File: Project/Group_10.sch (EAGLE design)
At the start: 20 parts, among them J1 POWER_JACKPTH_LOCK, U1 +12v, U4 TMUX1208

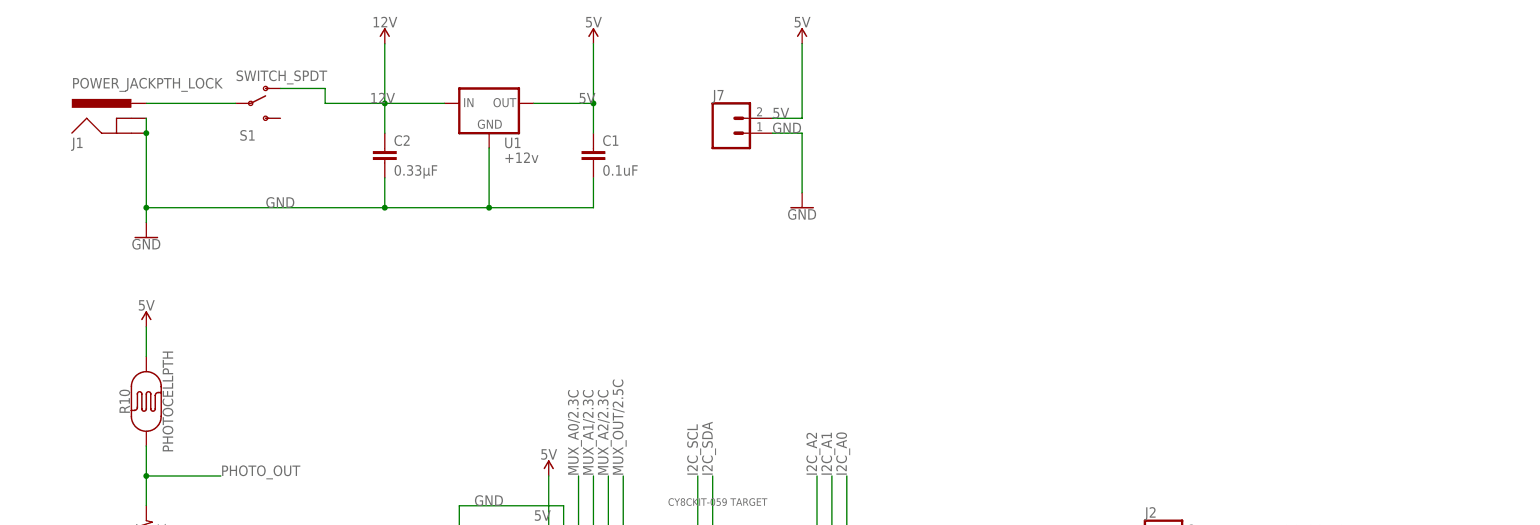
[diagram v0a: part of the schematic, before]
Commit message: Added device TCA9546A to schematic and added value to R1
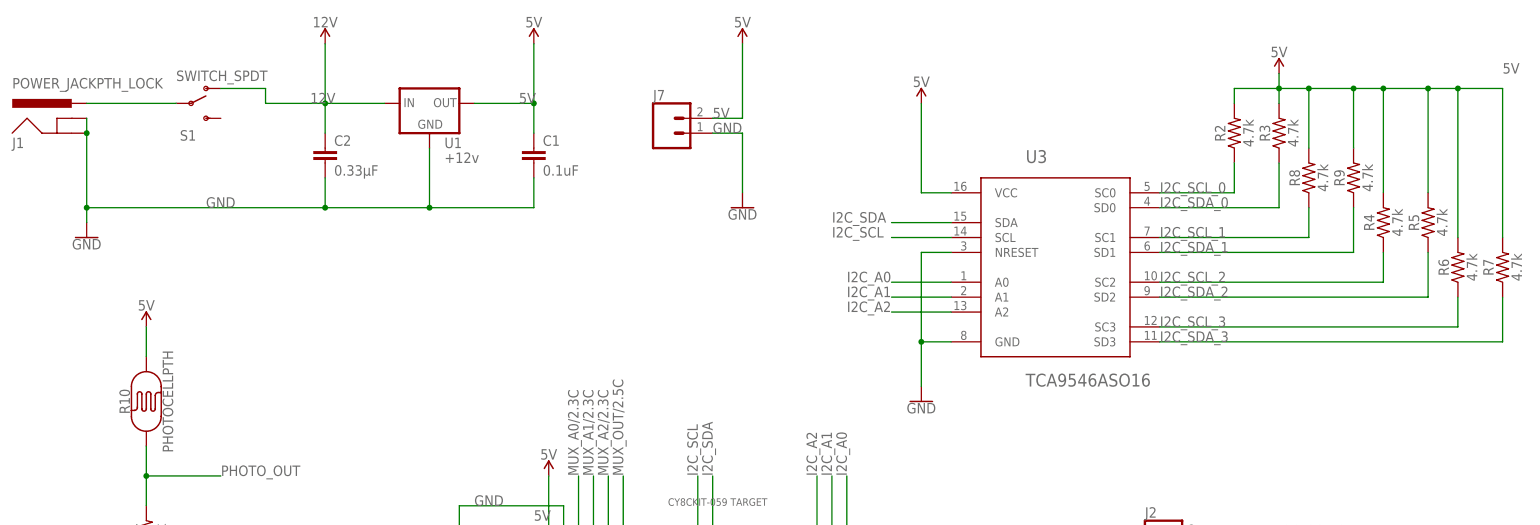
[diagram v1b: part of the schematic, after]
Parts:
- added R2, R3, R4, R5, R6, R7, R8, R9: 4.7k, SparkFun-Resistors:4.7KOHM-0603-1/10W-1%
- added U3: TCA9546ASO16, Group_10_Library:TCA9546ASO16
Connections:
- net 5V: now also R2.2, R3.2, R4.2, R5.2, R6.2, R7.2, R8.2, R9.2, U3.VCC
- net GND: now also U3.GND, U3.NRESET
- net I2C_A0: now also U3.A0
- net I2C_A1: now also U3.A1
- net I2C_A2: now also U3.A2
- net I2C_SCL: now also U3.SCL
- net I2C_SCL_0: now also R2.1, U3.SC0
- net I2C_SCL_1: now also R8.1, U3.SC1
- net I2C_SCL_2: now also R4.1, U3.SC2
- net I2C_SCL_3: now also R6.1, U3.SC3
- net I2C_SDA: now also U3.SDA
- net I2C_SDA_0: now also R3.1, U3.SD0
- net I2C_SDA_1: now also R9.1, U3.SD1
- net I2C_SDA_2: now also R5.1, U3.SD2
- net I2C_SDA_3: now also R7.1, U3.SD3
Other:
- moved on the sheet: C1, C2, J1, J7, S1, U1

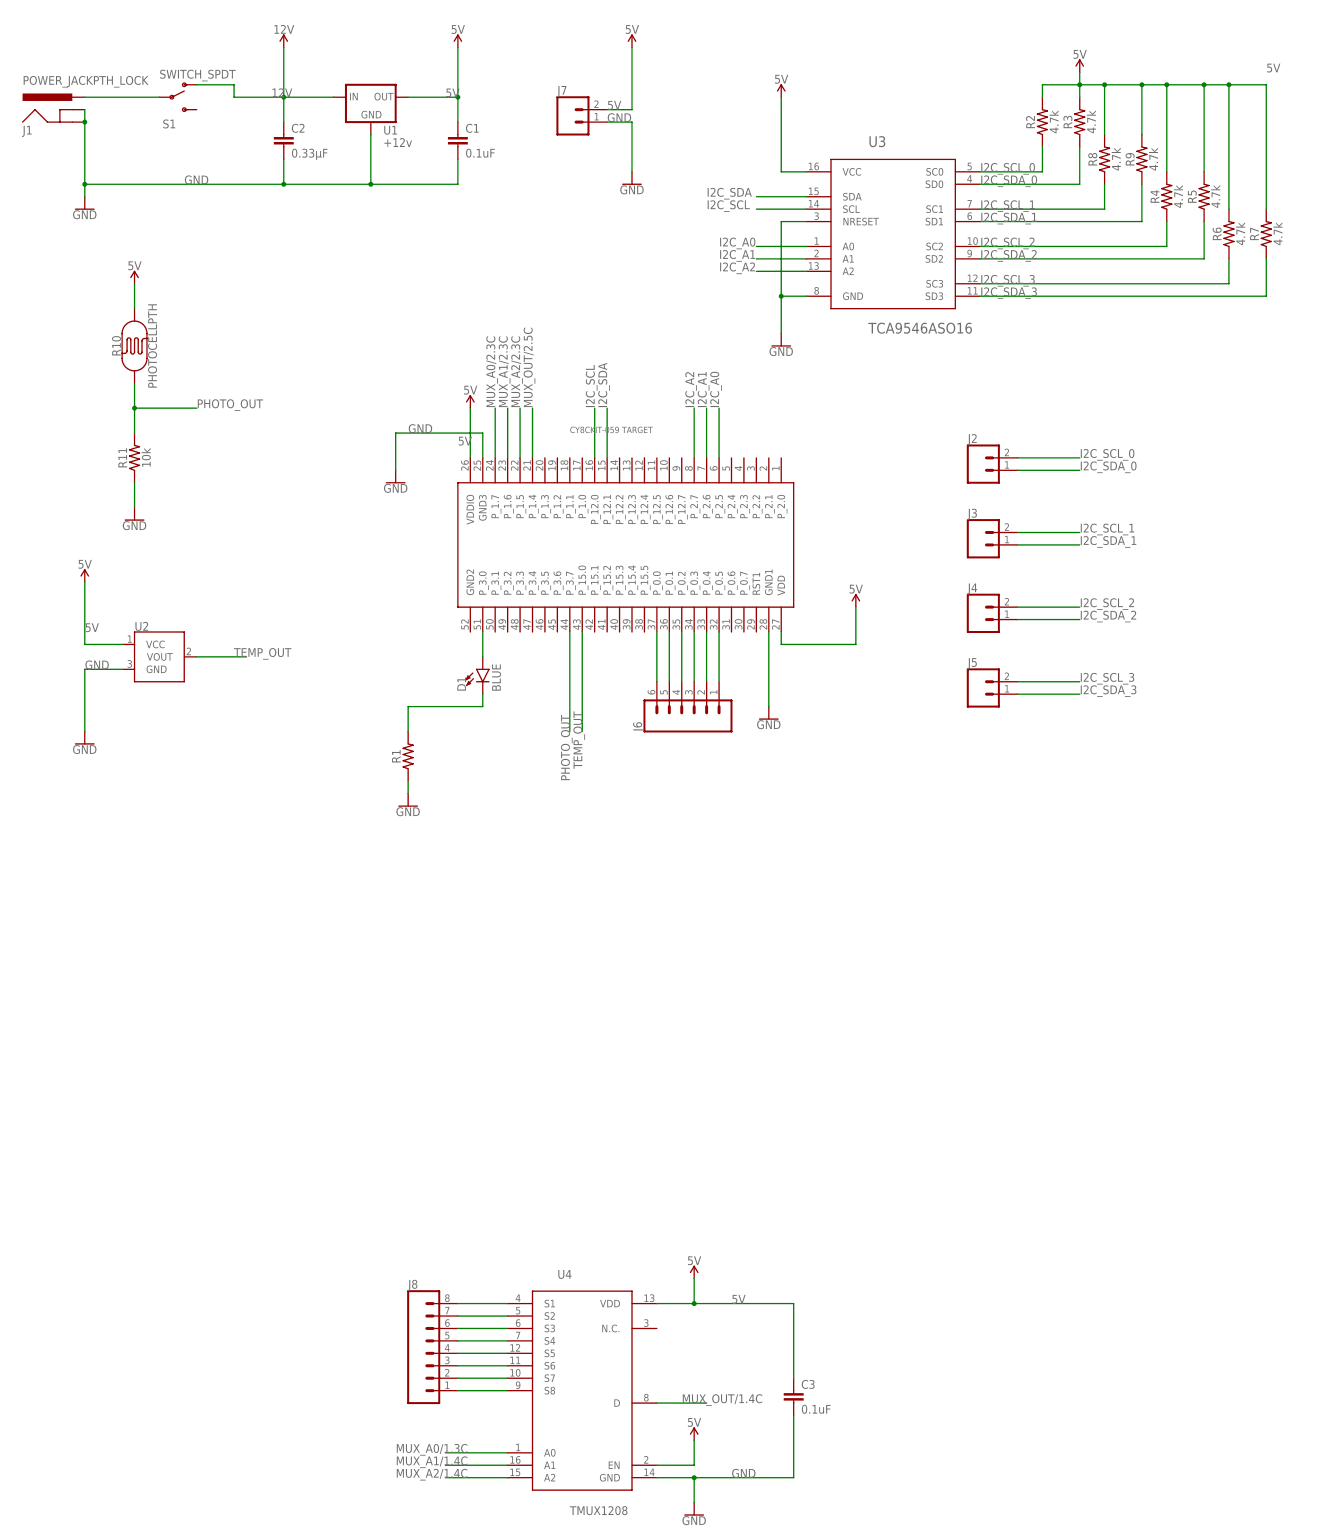
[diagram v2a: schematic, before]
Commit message: added comments to the schematic
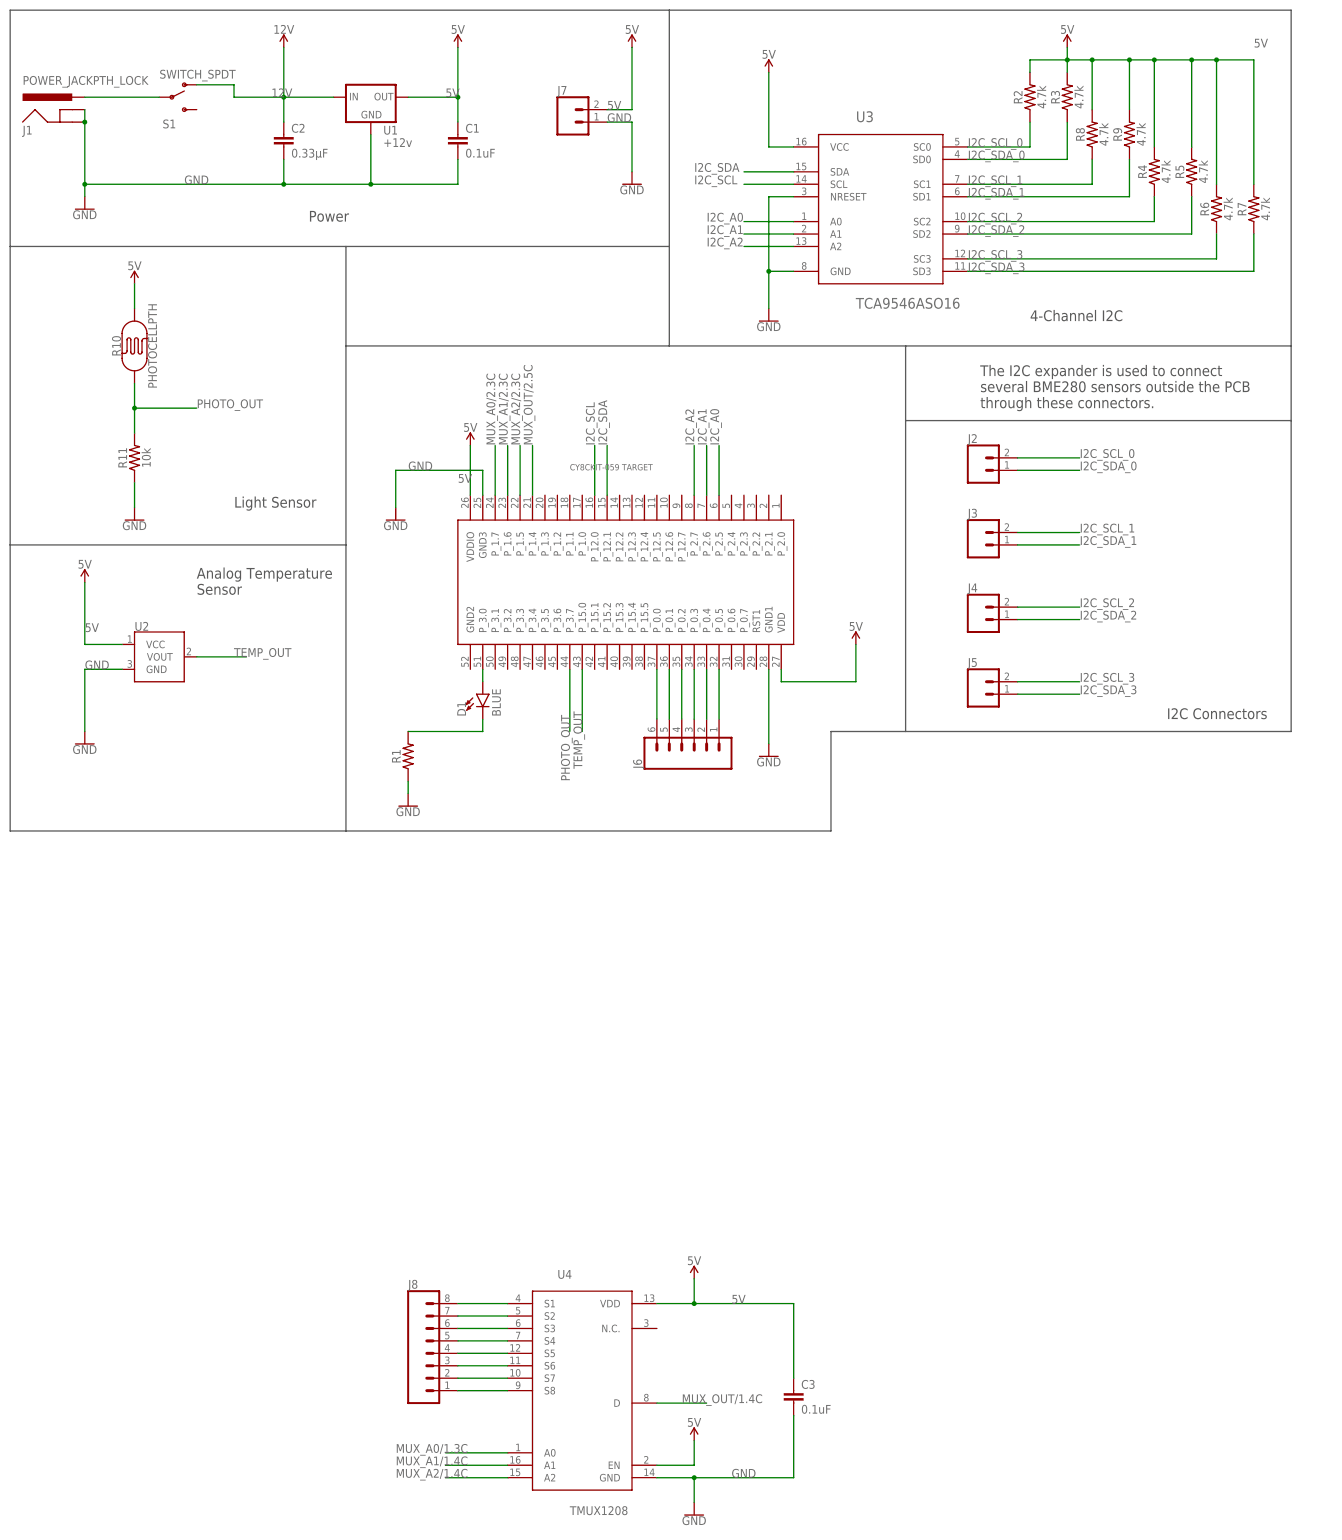
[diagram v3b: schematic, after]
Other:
- note added: "4-Channel I2C"
- note added: "Analog Temperature Sensor"
- note added: "I2C Connectors"
- note added: "Light Sensor"
- note added: "Power"
- note added: "The I2C expander is used to connect several BME280 sensors outside the PCB through these connectors."
- moved on the sheet: D1, J6, R2, R3, R4, R5, R6, R7, R8, R9, U3

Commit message: Corrected an error in schematic that caused some MUX connections to not be reflected in the board. Then connected them in the board
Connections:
- removed net MUX_A0/1.3C: U4.A0
- removed net MUX_A0/2.3C: U$2.P_1.7
- removed net MUX_A1/1.4C: U4.A1
- removed net MUX_A1/2.3C: U$2.P_1.6
- removed net MUX_A2/1.4C: U4.A2
- removed net MUX_A2/2.3C: U$2.P_1.5
- removed net MUX_OUT/1.4C: U4.D
- removed net MUX_OUT/2.5C: U$2.P_1.4
- new net MUX_A0: U$2.P_1.7, U4.A0
- new net MUX_A1: U$2.P_1.6, U4.A1
- new net MUX_A2: U$2.P_1.5, U4.A2
- new net MUX_OUT: U$2.P_1.4, U4.D
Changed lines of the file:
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@@
 </segment>
 </net>
-<net name="MUX_OUT/2.5C" class="0">
+<net name="MUX_OUT" class="0">
 <segment>
 <pinref part="U$2" gate="G$1" pin="P_1.4"/>
@@
 <label x="114.3" y="76.2" size="1.778" layer="95" rot="R90"/>
 </segment>
+<segment>
+<pinref part="U4" gate="G$1" pin="D"/>
+<wire x1="139.7" y1="-119.38" x2="149.86" y2="-119.38" width="0.1524" layer="91"/>
+<label x="144.78" y="-119.38" size="1.778" layer="95"/>
+</segment>
 </net>
-<net name="MUX_A2/2.3C" class="0">
+<net name="MUX_A2" class="0">
 <segment>
 <pinref part="U$2" gate="G$1" pin="P_1.5"/>
@@
 <label x="111.76" y="76.2" size="1.778" layer="95" rot="R90"/>
 </segment>
+<segment>
+<pinref part="U4" gate="G$1" pin="A2"/>
+<wire x1="109.22" y1="-134.62" x2="96.52" y2="-134.62" width="0.1524" layer="91"/>
+<label x="86.36" y="-134.62" size="1.778" layer="95"/>
+</segment>
 </net>
-<net name="MUX_A1/2.3C" class="0">
+<net name="MUX_A1" class="0">
 <segment>
 <pinref part="U$2" gate="G$1" pin="P_1.6"/>
@@
 <label x="109.22" y="76.2" size="1.778" layer="95" rot="R90"/>
 </segment>
+<segment>
+<pinref part="U4" gate="G$1" pin="A1"/>
+<wire x1="109.22" y1="-132.08" x2="96.52" y2="-132.08" width="0.1524" layer="91"/>
+<label x="86.36" y="-132.08" size="1.778" layer="95"/>
+</segment>
 </net>
-<net name="MUX_A0/2.3C" class="0">
+<net name="MUX_A0" class="0">
 <segment>
 <pinref part="U$2" gate="G$1" pin="P_1.7"/>
 <wire x1="106.68" y1="66.04" x2="106.68" y2="76.2" width="0.1524" layer="91"/>
 <label x="106.68" y="76.2" size="1.778" layer="95" rot="R90"/>
+</segment>
+<segment>
+<pinref part="U4" gate="G$1" pin="A0"/>
+<wire x1="109.22" y1="-129.54" x2="96.52" y2="-129.54" width="0.1524" layer="91"/>
+<label x="86.36" y="-129.54" size="1.778" layer="95"/>
 </segment>
 </net>
@@
 </segment>
 </net>
-<net name="MUX_OUT/1.4C" class="0">
-<segment>
-<pinref part="U4" gate="G$1" pin="D"/>
-<wire x1="139.7" y1="-119.38" x2="149.86" y2="-119.38" width="0.1524" layer="91"/>
-<label x="144.78" y="-119.38" size="1.778" layer="95"/>
-</segment>
-</net>
-<net name="MUX_A0/1.3C" class="0">
-<segment>
-<pinref part="U4" gate="G$1" pin="A0"/>
-<wire x1="109.22" y1="-129.54" x2="96.52" y2="-129.54" width="0.1524" layer="91"/>
-<label x="86.36" y="-129.54" size="1.778" layer="95"/>
-</segment>
-</net>
-<net name="MUX_A1/1.4C" class="0">
-<segment>
-<pinref part="U4" gate="G$1" pin="A1"/>
-<wire x1="109.22" y1="-132.08" x2="96.52" y2="-132.08" width="0.1524" layer="91"/>
-<label x="86.36" y="-132.08" size="1.778" layer="95"/>
-</segment>
-</net>
-<net name="MUX_A2/1.4C" class="0">
-<segment>
-<pinref part="U4" gate="G$1" pin="A2"/>
-<wire x1="109.22" y1="-134.62" x2="96.52" y2="-134.62" width="0.1524" layer="91"/>
-<label x="86.36" y="-134.62" size="1.778" layer="95"/>
-</segment>
-</net>
